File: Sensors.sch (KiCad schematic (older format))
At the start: 50 parts, among them CON1 CONSOLE, P1 CONN_02X20, P10 CBUS, P11 I2C0, P12 I2C0, P13 I2C1, P14 I2C1, P7 96B_SPI, Q2 CJ2305, Q3 CJ2305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

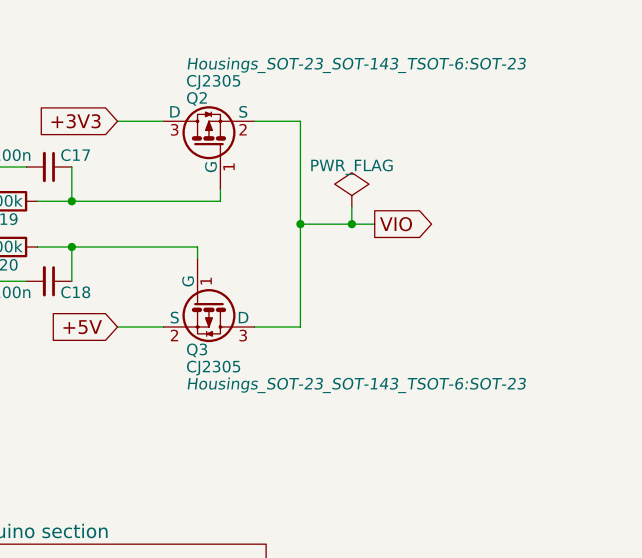
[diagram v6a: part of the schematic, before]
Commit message: Fix errors in part number fields
Minor changes to the part number fields, and an update to a footprint
selection

Signed-off-by: Grant Likely <grant.likely@linaro.org>
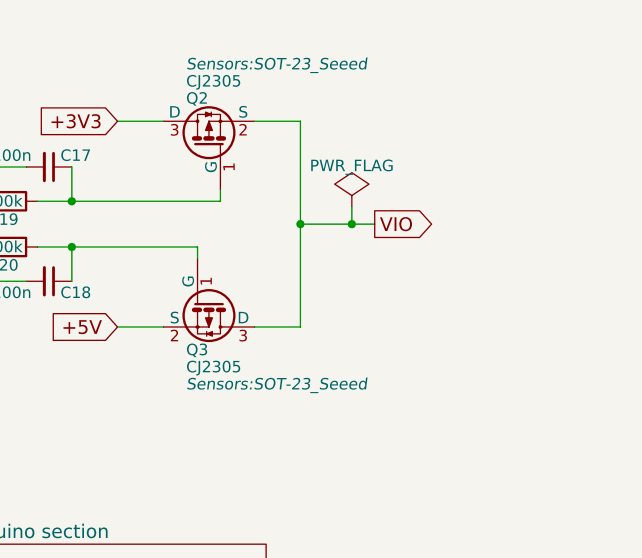
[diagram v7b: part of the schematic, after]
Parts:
- Q2, Q3: footprint Housings_SOT-23_SOT-143_TSOT-6:SOT-23 -> Sensors:SOT-23_Seeed
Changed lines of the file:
@@
 F 0 "Q2" V 10350 1350 50  0000 R CNN
 F 1 "CJ2305" V 10425 1350 50  0000 R CNN
-F 2 "Housings_SOT-23_SOT-143_TSOT-6:SOT-23" V 10500 1350 50  0000 R CIN
+F 2 "Sensors:SOT-23_Seeed" V 10500 1350 50  0000 R CIN
 F 3 "" H 10150 1250 50  0000 L CNN
 F 4 "305030014" H 10150 1250 60  0001 C CNN "Seeed SKU"
@@
 F 0 "Q3" V 10350 1850 50  0000 L CNN
 F 1 "CJ2305" V 10425 1850 50  0000 L CNN
-F 2 "Housings_SOT-23_SOT-143_TSOT-6:SOT-23" V 10500 1850 50  0000 L CIN
+F 2 "Sensors:SOT-23_Seeed" V 10500 1850 50  0000 L CIN
 F 3 "" H 10150 1950 50  0000 L CNN
 F 4 "305030014" H 10150 1950 60  0001 C CNN "Seeed SKU"

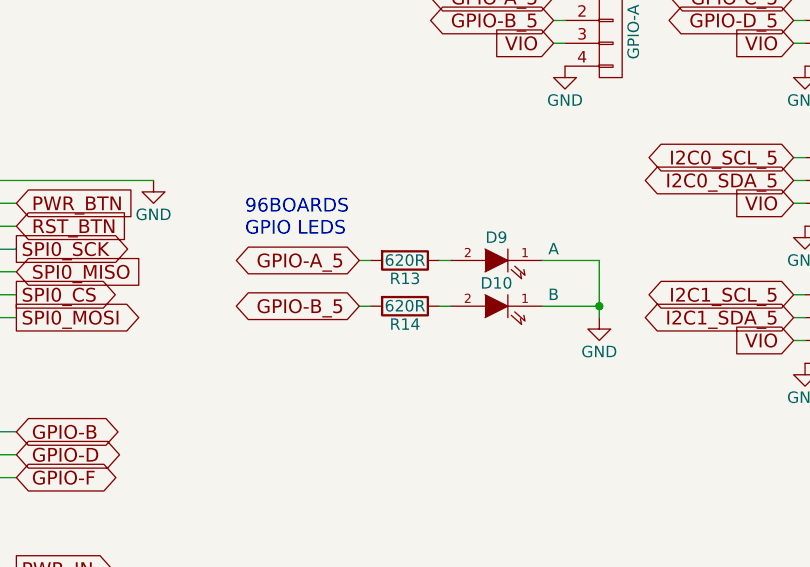
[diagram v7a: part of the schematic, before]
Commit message: Change LED resistor values to 1k
At 5V, a 620ohm resistor makes the LEDs too bright.

Signed-off-by: Grant Likely <grant.likely@linaro.org>
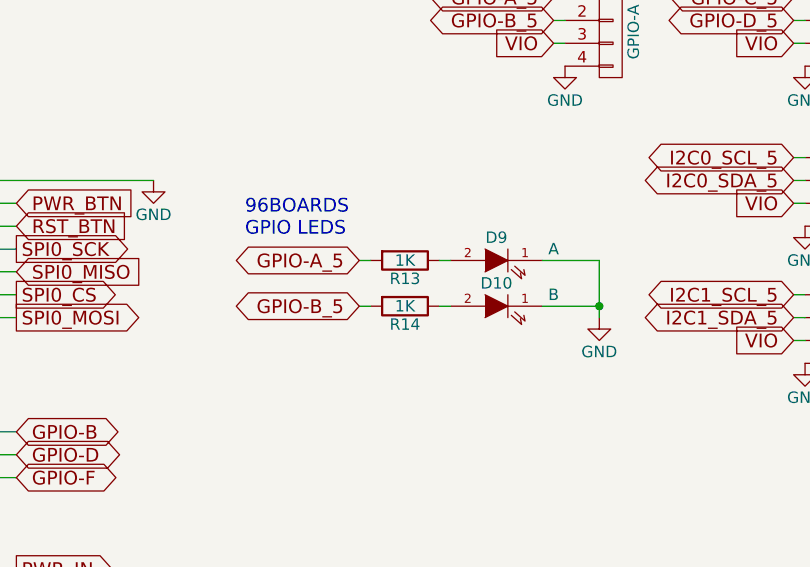
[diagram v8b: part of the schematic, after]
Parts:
- R13, R14: value 620R -> 1K; Mfr Part # RC0603JR-07620RL -> RC0402JR-071KL; Seeed SKU 301010210 -> 301010006
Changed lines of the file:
@@
 P 7900 6050
 F 0 "R14" V 7980 6050 50  0000 C CNN
-F 1 "620R" V 7900 6050 50  0000 C CNN
+F 1 "1K" V 7900 6050 50  0000 C CNN
 F 2 "Sensors:R_0603_Seeed" V 7830 6050 30  0001 C CNN
 F 3 "" H 7900 6050 30  0000 C CNN
-F 4 "301010210" H 2050 900 60  0001 C CNN "Seeed SKU"
+F 4 "301010006" H 2050 900 60  0001 C CNN "Seeed SKU"
 F 5 "Yageo" H 2050 900 60  0001 C CNN "Mfr"
-F 6 "RC0603JR-07620RL" H 2050 900 60  0001 C CNN "Mfr Part #"
+F 6 "RC0402JR-071KL" H 2050 900 60  0001 C CNN "Mfr Part #"
 	1    7900 6050
 	0    1    1    0
@@
 P 7900 5850
 F 0 "R13" V 7980 5850 50  0000 C CNN
-F 1 "620R" V 7900 5850 50  0000 C CNN
+F 1 "1K" V 7900 5850 50  0000 C CNN
 F 2 "Sensors:R_0603_Seeed" V 7830 5850 30  0001 C CNN
 F 3 "" H 7900 5850 30  0000 C CNN
-F 4 "301010210" H 1900 700 60  0001 C CNN "Seeed SKU"
+F 4 "301010006" H 1900 700 60  0001 C CNN "Seeed SKU"
 F 5 "Yageo" H 1900 700 60  0001 C CNN "Mfr"
-F 6 "RC0603JR-07620RL" H 1900 700 60  0001 C CNN "Mfr Part #"
+F 6 "RC0402JR-071KL" H 1900 700 60  0001 C CNN "Mfr Part #"
 	1    7900 5850
 	0    1    1    0
